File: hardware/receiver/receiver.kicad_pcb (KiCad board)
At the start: 2 copper layers, 68.6 x 53.3 mm, 21 parts, among them J1 Input, J3 LED_OUT

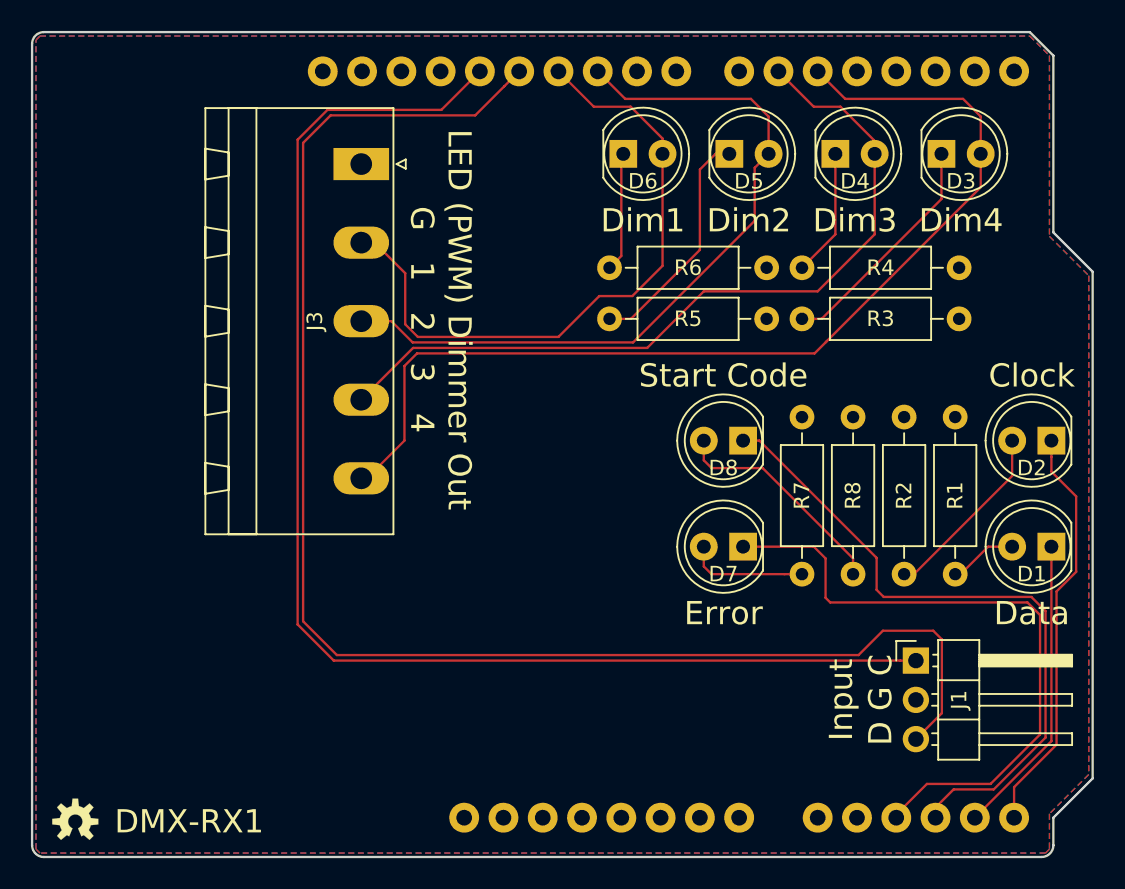
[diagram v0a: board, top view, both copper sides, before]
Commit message: TX1 1.2, RX1 1.2 Move Clock LED to avoid ICSP connector. Align TX Fast/Slo clock LEDS and RX start code/error LEDs.
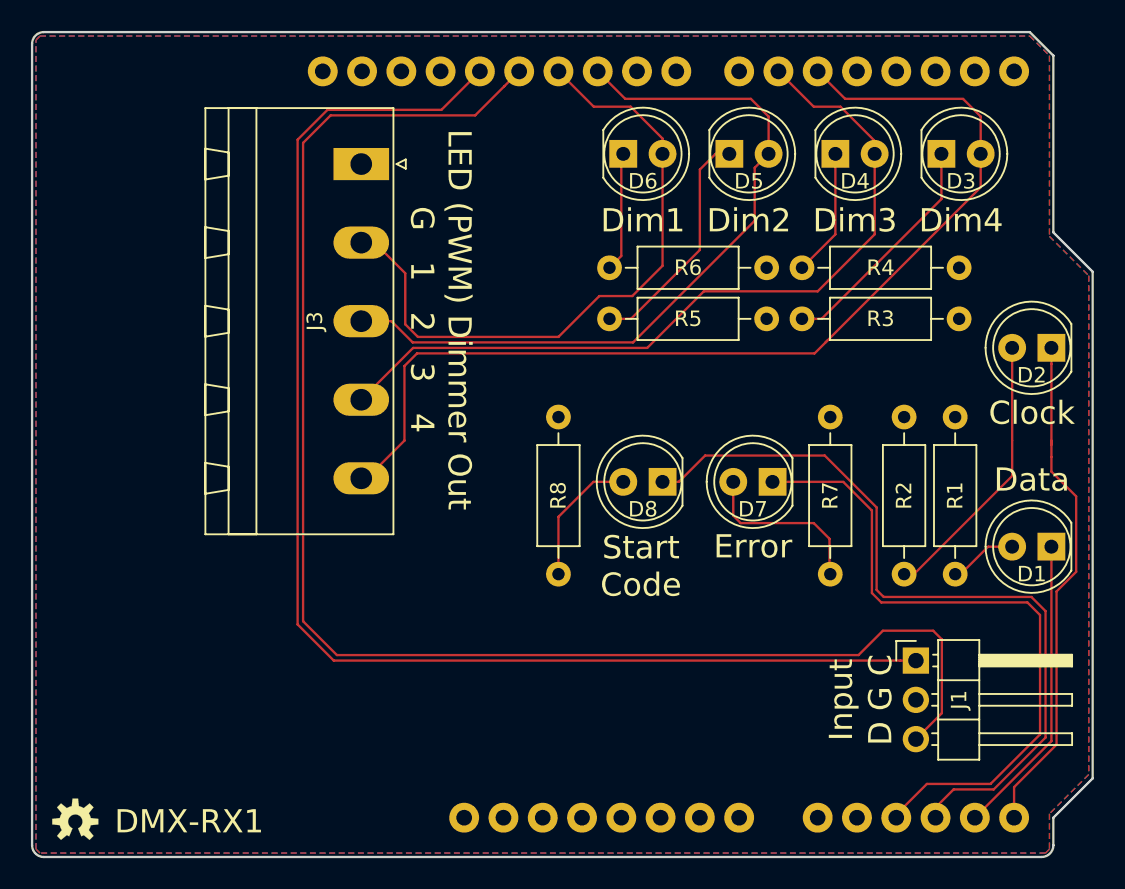
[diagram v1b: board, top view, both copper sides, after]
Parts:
- moved R8 19.1 mm to (150.4, 88.1)
- moved D2 6.00 mm to (182.2, 83.7)
- moved D8 5.85 mm to (157.1, 92.3)
- moved D7 4.60 mm to (164.2, 92.3)
- moved R7 1.83 mm to (167.9, 88.1)
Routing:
- net /~SC: track 43.2 -> 50.6 mm
- net /~CLOCK: track 26.7 -> 33.0 mm
- net Net-(D2-Pad2): track 11.9 -> 17.9 mm
- net Net-(D8-Pad2): track 14.6 -> 8.84 mm
- net Net-(D7-Pad2): track 7.83 -> 11.3 mm
- net /~ERR: track 41.9 -> 43.4 mm
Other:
- board text added: "DMX-RX1, Rev 1.2 Crazy Giraffe Software"
- board text removed: "DMX-RX1, Rev 1.1 Crazy Giraffe Software"

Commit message: Add RXCLK to D9 connection for Leonardo PCINT5.
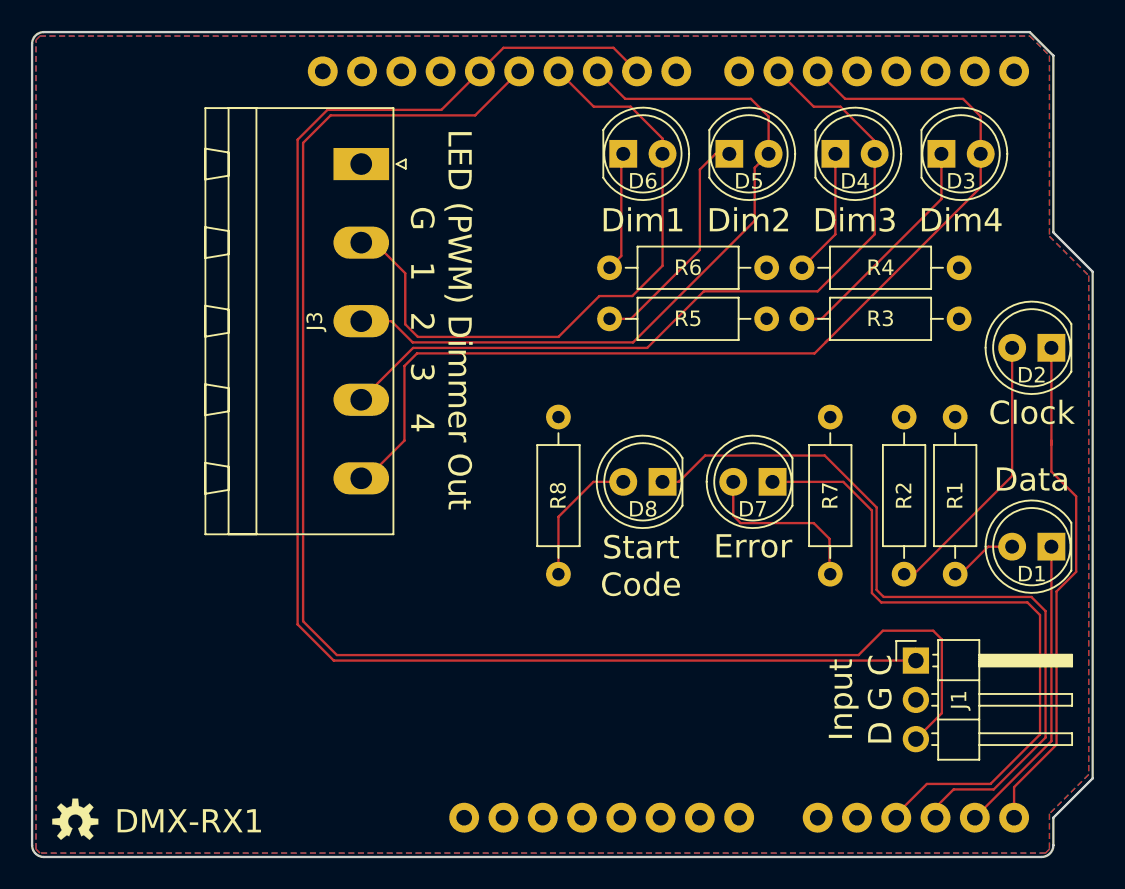
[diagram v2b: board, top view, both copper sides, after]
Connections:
- A1 pad 24: Net-(A1-Pad24) -> /RXCLK
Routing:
- net /RXCLK: track 87.2 -> 98.7 mm
